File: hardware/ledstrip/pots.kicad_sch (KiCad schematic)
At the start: 3 parts

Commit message: Add label on nodes.
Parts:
- RV1: value R_Potentiometer -> Pot_R
- RV2: value R_Potentiometer -> Pot_G
- RV3: value R_Potentiometer -> Pot_B
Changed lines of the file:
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@@
 			)
 		)
-		(property "Value" "R_Potentiometer"
+		(property "Value" "Pot_G"
 			(at 137.16 95.2499 0)
 			(effects
@@
 			)
 		)
-		(property "Value" "R_Potentiometer"
+		(property "Value" "Pot_B"
 			(at 137.16 83.8199 0)
 			(effects
@@
 			)
 		)
-		(property "Value" "R_Potentiometer"
+		(property "Value" "Pot_R"
 			(at 137.16 107.9499 0)
 			(effects

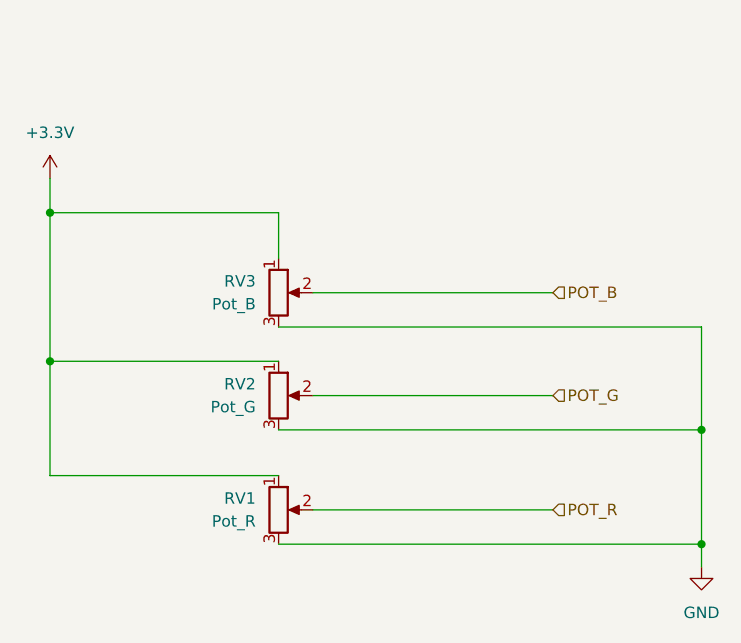
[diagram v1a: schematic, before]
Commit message: Fix ILIM_HIZ setting on BQ25703A
Add comments on schematics about hardware configuration.
Setup a early stable 2.5V from REGN to setup ILIM_HIZ correctly.
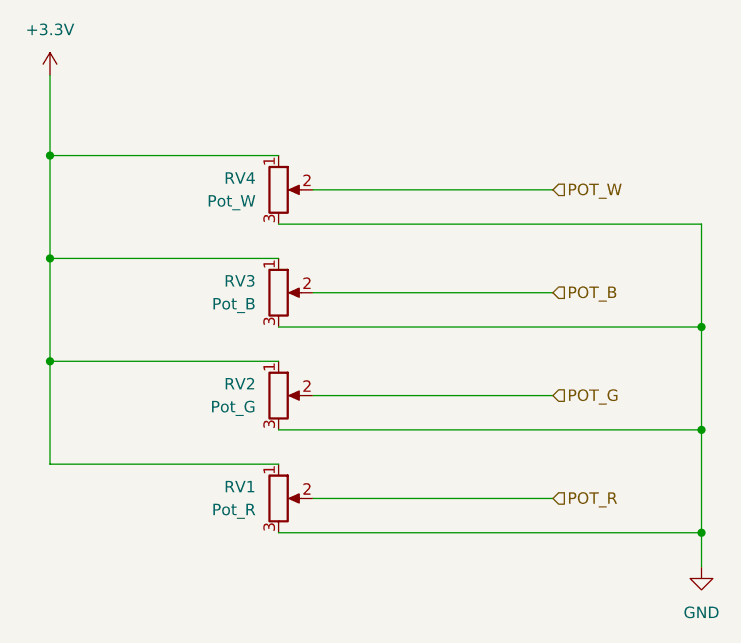
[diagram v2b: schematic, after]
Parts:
- added RV4: Pot_W, Potentiometer_THT:Potentiometer_Bourns_PTV09A-1_Single_Vertical, symbol Device:R_Potentiometer
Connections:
- net +3.3V: now also RV4.1
- net GND: now also RV4.3
- new net POT_W: RV4.2
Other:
- moved on the sheet: RV1
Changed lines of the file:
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@@
 	)
 	(junction
-		(at 186.69 110.49)
+		(at 114.3 67.31)
 		(diameter 0)
 		(color 0 0 0 0)
 	)
 	(junction
-		(at 114.3 73.66)
+		(at 114.3 78.74)
 		(diameter 0)
 		(color 0 0 0 0)
 	)
-	(wire
-		(pts
-			(xy 186.69 110.49) (xy 186.69 113.03)
-		)
-		(stroke
-			(width 0)
-			(type default)
-		)
-	)
-	(wire
-		(pts
-			(xy 186.69 97.79) (xy 186.69 110.49)
-		)
-		(stroke
-			(width 0)
-			(type default)
-		)
-	)
-	(wire
-		(pts
-			(xy 114.3 73.66) (xy 114.3 69.85)
-		)
-		(stroke
-			(width 0)
-			(type default)
-		)
-	)
-	(wire
-		(pts
-			(xy 114.3 102.87) (xy 139.7 102.87)
-		)
-		(stroke
-			(width 0)
-			(type default)
-		)
-	)
-	(wire
-		(pts
-			(xy 139.7 73.66) (xy 139.7 78.74)
-		)
-		(stroke
-			(width 0)
-			(type default)
-		)
-	)
-	(wire
-		(pts
-			(xy 139.7 110.49) (xy 186.69 110.49)
+	(junction
+		(at 186.69 109.22)
+		(diameter 0)
+		(color 0 0 0 0)
+	)
+	(junction
+		(at 186.69 86.36)
+		(diameter 0)
+		(color 0 0 0 0)
+	)
+	(wire
+		(pts
+			(xy 186.69 97.79) (xy 186.69 109.22)
+		)
+		(stroke
+			(width 0)
+			(type default)
+		)
+	)
+	(wire
+		(pts
+			(xy 114.3 58.42) (xy 114.3 67.31)
+		)
+		(stroke
+			(width 0)
+			(type default)
+		)
+	)
+	(wire
+		(pts
+			(xy 114.3 101.6) (xy 139.7 101.6)
+		)
+		(stroke
+			(width 0)
+			(type default)
+		)
+	)
+	(wire
+		(pts
+			(xy 139.7 109.22) (xy 186.69 109.22)
+		)
+		(stroke
+			(width 0)
+			(type default)
+		)
+	)
+	(wire
+		(pts
+			(xy 114.3 67.31) (xy 139.7 67.31)
 		)
 		(stroke
@@
 	(wire
 		(pts
-			(xy 114.3 90.17) (xy 114.3 102.87)
+			(xy 114.3 90.17) (xy 114.3 101.6)
 		)
 		(stroke
@@
 	(wire
 		(pts
-			(xy 114.3 73.66) (xy 114.3 90.17)
-		)
-		(stroke
-			(width 0)
-			(type default)
-		)
-	)
-	(wire
-		(pts
-			(xy 143.51 106.68) (xy 170.18 106.68)
+			(xy 143.51 71.12) (xy 170.18 71.12)
+		)
+		(stroke
+			(width 0)
+			(type default)
+		)
+	)
+	(wire
+		(pts
+			(xy 143.51 105.41) (xy 170.18 105.41)
+		)
+		(stroke
+			(width 0)
+			(type default)
+		)
+	)
+	(wire
+		(pts
+			(xy 186.69 74.93) (xy 186.69 86.36)
+		)
+		(stroke
+			(width 0)
+			(type default)
+		)
+	)
+	(wire
+		(pts
+			(xy 114.3 67.31) (xy 114.3 78.74)
 		)
 		(stroke
@@
 	(wire
 		(pts
-			(xy 114.3 73.66) (xy 139.7 73.66)
-		)
-		(stroke
-			(width 0)
-			(type default)
-		)
-	)
-	(wire
-		(pts
 			(xy 143.51 93.98) (xy 170.18 93.98)
 		)
@@
 	(wire
 		(pts
+			(xy 139.7 74.93) (xy 186.69 74.93)
+		)
+		(stroke
+			(width 0)
+			(type default)
+		)
+	)
+	(wire
+		(pts
 			(xy 186.69 86.36) (xy 186.69 97.79)
 		)
@@
 	(wire
 		(pts
+			(xy 186.69 109.22) (xy 186.69 113.03)
+		)
+		(stroke
+			(width 0)
+			(type default)
+		)
+	)
+	(wire
+		(pts
 			(xy 143.51 82.55) (xy 170.18 82.55)
+		)
+		(stroke
+			(width 0)
+			(type default)
+		)
+	)
+	(wire
+		(pts
+			(xy 114.3 78.74) (xy 114.3 90.17)
+		)
+		(stroke
+			(width 0)
+			(type default)
+		)
+	)
+	(wire
+		(pts
+			(xy 114.3 78.74) (xy 139.7 78.74)
 		)
 		(stroke
@@
 		)
 	)
+	(hierarchical_label "POT_W"
+		(shape input)
+		(at 170.18 71.12 0)
+		(effects
+			(font
+				(size 1.27 1.27)
+			)
+			(justify left)
+		)
+	)
 	(hierarchical_label "POT_R"
 		(shape input)
-		(at 170.18 106.68 0)
+		(at 170.18 105.41 0)
 		(effects
 			(font
@@
 	(symbol
 		(lib_id "Device:R_Potentiometer")
+		(at 139.7 71.12 0)
+		(unit 1)
+		(exclude_from_sim no)
+		(in_bom yes)
+		(on_board yes)
+		(dnp no)
+		(fields_autoplaced yes)
+		(property "Reference" "RV4"
+			(at 137.16 69.8499 0)
+			(effects
+				(font
+					(size 1.27 1.27)
+				)
+				(justify right)
+			)
+		)
+		(property "Value" "Pot_W"
+			(at 137.16 72.3899 0)
+			(effects
+				(font
+					(size 1.27 1.27)
+				)
+				(justify right)
+			)
+		)
+		(property "Footprint" "Potentiometer_THT:Potentiometer_Bourns_PTV09A-1_Single_Vertical"
+			(at 139.7 71.12 0)
+			(effects
+				(font
+					(size 1.27 1.27)
+				)
+				(hide yes)
+			)
+		)
+		(property "Datasheet" "https://www.bourns.com/docs/product-datasheets/PTV09.pdf"
+			(at 139.7 71.12 0)
+			(effects
+				(font
+					(size 1.27 1.27)
+				)
+				(hide yes)
+			)
+		)
+		(property "Description" "Potentiometer"
+			(at 139.7 71.12 0)
+			(effects
+				(font
+					(size 1.27 1.27)
+				)
+				(hide yes)
+			)
+		)
+		(property "Distributor Link 1" "https://www.mouser.fr/ProductDetail/Bourns/PTV09A-6030U-B103?qs=pxDZlBjcsCisCJhLa2B%2FpQ%3D%3D"
+			(at 139.7 71.12 0)
+			(effects
+				(font
+					(size 1.27 1.27)
+				)
+				(hide yes)
+			)
+		)
+		(property "Distributor Link 2" "https://www.digikey.be/en/products/detail/bourns-inc/PTV09A-6030U-B103/6153494"
+			(at 139.7 71.12 0)
+			(effects
+				(font
+					(size 1.27 1.27)
+				)
+				(hide yes)
+			)
+		)
+		(pin "3"
+		)
+		(pin "1"
+		)
+		(pin "2"
+		)
+		(instances
+			(project "ledstrip"
+				(path "/dcb997ee-94c4-4df2-ba22-0e091735ddd7/0b9dc6db-254f-4d56-b53f-9075578fa80e"
+					(reference "RV4")
+					(unit 1)
+				)
+			)
+		)
+	)
+	(symbol
+		(lib_id "Device:R_Potentiometer")
 		(at 139.7 82.55 0)
 		(unit 1)
@@
 	(symbol
 		(lib_id "power:+3.3V")
-		(at 114.3 69.85 0)
+		(at 114.3 58.42 0)
 		(unit 1)
 		(exclude_from_sim no)
@@
 		(fields_autoplaced yes)
 		(property "Reference" "#PWR013"
-			(at 114.3 73.66 0)
+			(at 114.3 62.23 0)
 			(effects
 				(font
@@
 		)
 		(property "Value" "+3.3V"
-			(at 114.3 64.77 0)
+			(at 114.3 53.34 0)
 			(effects
 				(font
@@
 		)
 		(property "Footprint" ""
-			(at 114.3 69.85 0)
+			(at 114.3 58.42 0)
 			(effects
 				(font
@@
 		)
 		(property "Datasheet" ""
-			(at 114.3 69.85 0)
+			(at 114.3 58.42 0)
 			(effects
 				(font
@@
 		)
 		(property "Description" "Power symbol creates a global label with name \"+3.3V\""
-			(at 114.3 69.85 0)
+			(at 114.3 58.42 0)
 			(effects
 				(font
@@
 	(symbol
 		(lib_id "Device:R_Potentiometer")
-		(at 139.7 106.68 0)
+		(at 139.7 105.41 0)
 		(unit 1)
 		(exclude_from_sim no)
@@
 		(fields_autoplaced yes)
 		(property "Reference" "RV1"
-			(at 137.16 105.4099 0)
+			(at 137.16 104.1399 0)
 			(effects
 				(font
@@
 		)
 		(property "Value" "Pot_R"
-			(at 137.16 107.9499 0)
+			(at 137.16 106.6799 0)
 			(effects
 				(font
@@
 		)
 		(property "Footprint" "Potentiometer_THT:Potentiometer_Bourns_PTV09A-1_Single_Vertical"
-			(at 139.7 106.68 0)
+			(at 139.7 105.41 0)
 			(effects
 				(font
@@
 		)
 		(property "Datasheet" "https://www.bourns.com/docs/product-datasheets/PTV09.pdf"
-			(at 139.7 106.68 0)
+			(at 139.7 105.41 0)
 			(effects
 				(font
@@
 		)
 		(property "Description" "Potentiometer"
-			(at 139.7 106.68 0)
+			(at 139.7 105.41 0)
 			(effects
 				(font
@@
 		)
 		(property "Distributor Link 1" "https://www.mouser.fr/ProductDetail/Bourns/PTV09A-6030U-B103?qs=pxDZlBjcsCisCJhLa2B%2FpQ%3D%3D"
-			(at 139.7 106.68 0)
+			(at 139.7 105.41 0)
 			(effects
 				(font
@@
 		)
 		(property "Distributor Link 2" "https://www.digikey.be/en/products/detail/bourns-inc/PTV09A-6030U-B103/6153494"
-			(at 139.7 106.68 0)
-			(effects
-				(font
+			(at 139.7 105.41 0)
+			(effects
+				(font

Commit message: Update schematics symbols fields for manufactrurer
Update BOM fields.
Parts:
- RV1, RV2, RV3, RV4: MPN (none) -> PTV09A-6030U-B103; Manufacturer (none) -> Bourns
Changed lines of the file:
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@@
+			)
+		)
+		(property "Manufacturer" "Bourns"
+			(at 139.7 93.98 0)
+			(effects
+				(font
+					(size 1.27 1.27)
+				)
+				(hide yes)
+			)
+		)
+		(property "MPN" "PTV09A-6030U-B103"
+			(at 139.7 93.98 0)
+			(effects
+				(font
+					(size 1.27 1.27)
+				)
+				(hide yes)
 			)
 		)
 		(property "Distributor Link 2" "https://www.digikey.be/en/products/detail/bourns-inc/PTV09A-6030U-B103/6153494"
+			(at 139.7 93.98 0)
+			(effects
+				(font
+					(size 1.27 1.27)
+				)
+				(hide yes)
+			)
+		)
+		(property "Disributor Link 1" ""
+			(at 139.7 93.98 0)
+			(effects
+				(font
+					(size 1.27 1.27)
+				)
+				(hide yes)
+			)
+		)
+		(property "Ditributor Link 1" ""
+			(at 139.7 93.98 0)
+			(effects
+				(font
+					(size 1.27 1.27)
+				)
+				(hide yes)
+			)
+		)
+		(property "Manufacturer Part Number" ""
 			(at 139.7 93.98 0)
 			(effects
@@
 			)
 		)
+		(property "Manufacturer" "Bourns"
+			(at 139.7 71.12 0)
+			(effects
+				(font
+					(size 1.27 1.27)
+				)
+				(hide yes)
+			)
+		)
+		(property "MPN" "PTV09A-6030U-B103"
+			(at 139.7 71.12 0)
+			(effects
+				(font
+					(size 1.27 1.27)
+				)
+				(hide yes)
+			)
+		)
 		(property "Distributor Link 2" "https://www.digikey.be/en/products/detail/bourns-inc/PTV09A-6030U-B103/6153494"
+			(at 139.7 71.12 0)
+			(effects
+				(font
+					(size 1.27 1.27)
+				)
+				(hide yes)
+			)
+		)
+		(property "Disributor Link 1" ""
+			(at 139.7 71.12 0)
+			(effects
+				(font
+					(size 1.27 1.27)
+				)
+				(hide yes)
+			)
+		)
+		(property "Ditributor Link 1" ""
+			(at 139.7 71.12 0)
+			(effects
+				(font
+					(size 1.27 1.27)
+				)
+				(hide yes)
+			)
+		)
+		(property "Manufacturer Part Number" ""
 			(at 139.7 71.12 0)
 			(effects
@@
 			)
 		)
+		(property "Manufacturer" "Bourns"
+			(at 139.7 82.55 0)
+			(effects
+				(font
+					(size 1.27 1.27)
+				)
+				(hide yes)
+			)
+		)
+		(property "MPN" "PTV09A-6030U-B103"
+			(at 139.7 82.55 0)
+			(effects
+				(font
+					(size 1.27 1.27)
+				)
+				(hide yes)
+			)
+		)
 		(property "Distributor Link 2" "https://www.digikey.be/en/products/detail/bourns-inc/PTV09A-6030U-B103/6153494"
+			(at 139.7 82.55 0)
+			(effects
+				(font
+					(size 1.27 1.27)
+				)
+				(hide yes)
+			)
+		)
+		(property "Disributor Link 1" ""
+			(at 139.7 82.55 0)
+			(effects
+				(font
+					(size 1.27 1.27)
+				)
+				(hide yes)
+			)
+		)
+		(property "Ditributor Link 1" ""
+			(at 139.7 82.55 0)
+			(effects
+				(font
+					(size 1.27 1.27)
+				)
+				(hide yes)
+			)
+		)
+		(property "Manufacturer Part Number" ""
 			(at 139.7 82.55 0)
 			(effects
@@
 			)
 		)
+		(property "Manufacturer" "Bourns"
+			(at 139.7 105.41 0)
+			(effects
+				(font
+					(size 1.27 1.27)
+				)
+				(hide yes)
+			)
+		)
+		(property "MPN" "PTV09A-6030U-B103"
+			(at 139.7 105.41 0)
+			(effects
+				(font
+					(size 1.27 1.27)
+				)
+				(hide yes)
+			)
+		)
 		(property "Distributor Link 2" "https://www.digikey.be/en/products/detail/bourns-inc/PTV09A-6030U-B103/6153494"
 			(at 139.7 105.41 0)
 			(effects
+				(font
+					(size 1.27 1.27)
+				)
+				(hide yes)
+			)
+		)
+		(property "Disributor Link 1" ""
+			(at 139.7 105.41 0)
+			(effects
+				(font
+					(size 1.27 1.27)
+				)
+				(hide yes)
+			)
+		)
+		(property "Ditributor Link 1" ""
+			(at 139.7 105.41 0)
+			(effects
+				(font
+					(size 1.27 1.27)
+				)
+				(hide yes)
+			)
+		)
+		(property "Manufacturer Part Number" ""
+			(at 139.7 105.41 0)
+			(effects
